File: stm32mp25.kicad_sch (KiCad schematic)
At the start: 0 parts

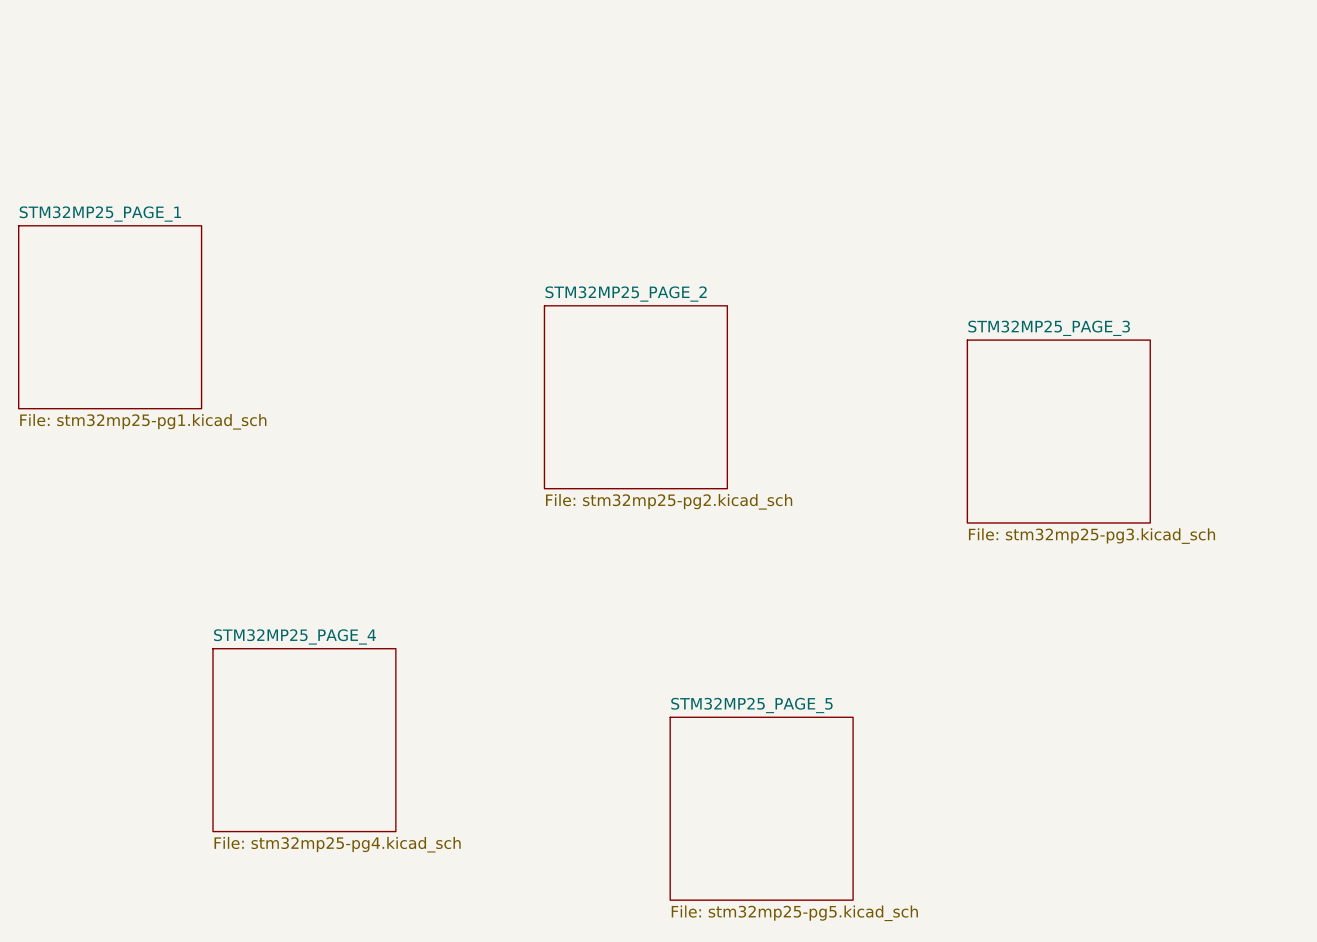
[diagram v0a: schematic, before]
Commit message: connected lpddr4 to mp
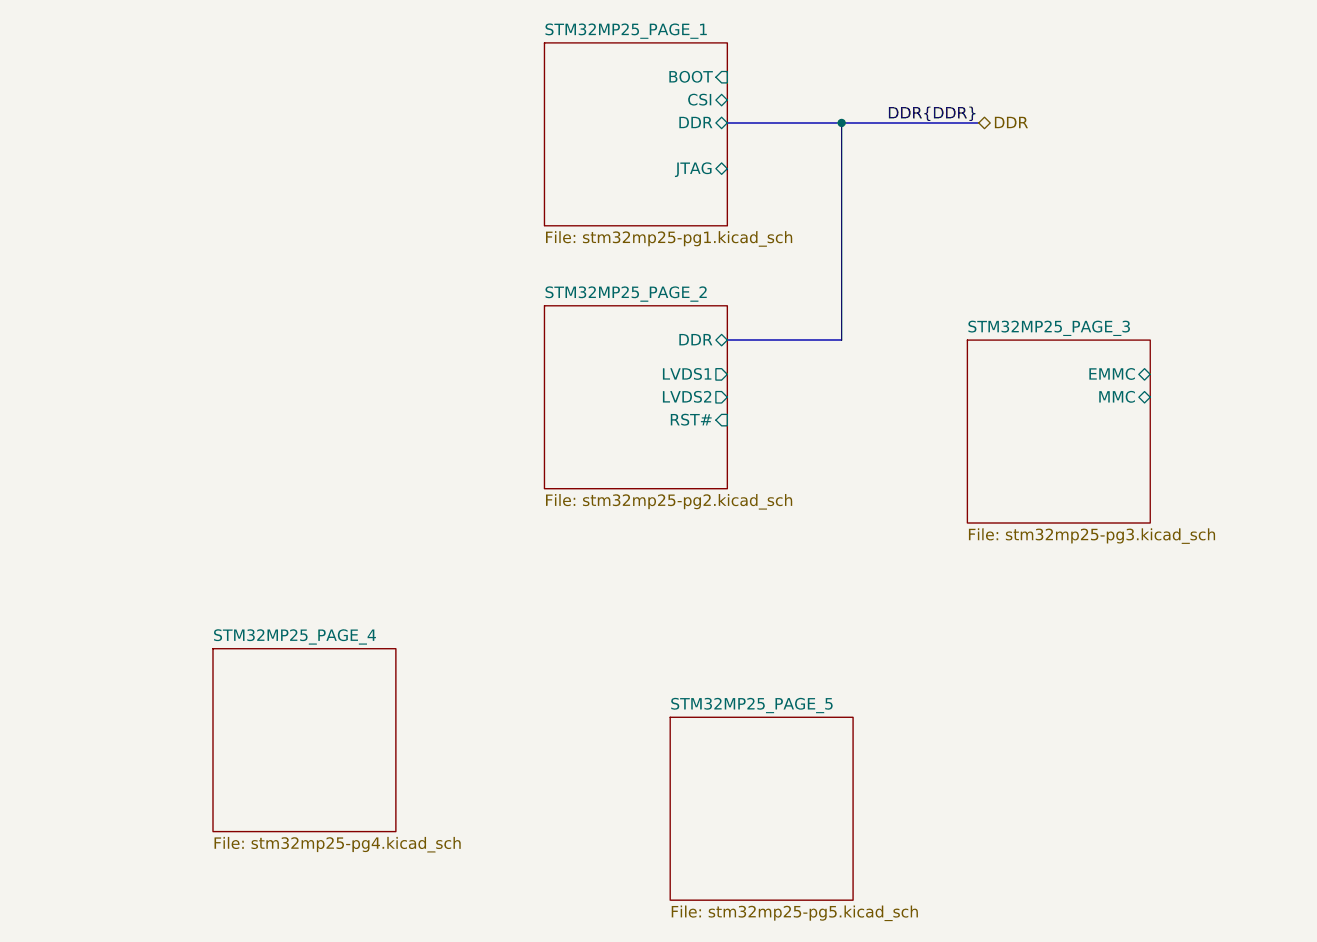
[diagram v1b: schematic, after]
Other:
- sheet STM32MP25_PAGE_1 ports: added BOOT, CSI, DDR, JTAG; removed none
- sheet STM32MP25_PAGE_2 ports: added DDR, LVDS1, LVDS2, RST#; removed none
- sheet STM32MP25_PAGE_3 ports: added EMMC, MMC; removed none
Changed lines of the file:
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@@
 	(generator_version "9.0")
 	(paper "A4")
+	(junction
+		(at 179.07 52.07)
+		(diameter 0)
+		(color 0 0 0 0)
+	)
+	(bus
+		(pts
+			(xy 179.07 52.07) (xy 194.31 52.07)
+		)
+		(stroke
+			(width 0)
+			(type default)
+		)
+	)
+	(bus
+		(pts
+			(xy 179.07 76.2) (xy 179.07 52.07)
+		)
+		(stroke
+			(width 0)
+			(type default)
+		)
+	)
+	(bus
+		(pts
+			(xy 179.07 52.07) (xy 166.37 52.07)
+		)
+		(stroke
+			(width 0)
+			(type default)
+		)
+	)
+	(bus
+		(pts
+			(xy 166.37 76.2) (xy 179.07 76.2)
+		)
+		(stroke
+			(width 0)
+			(type default)
+		)
+	)
+	(label "DDR{DDR}"
+		(at 184.15 52.07 0)
+		(effects
+			(font
+				(size 1.27 1.27)
+			)
+			(justify left bottom)
+		)
+	)
+	(hierarchical_label "DDR"
+		(shape bidirectional)
+		(at 194.31 52.07 0)
+		(effects
+			(font
+				(size 1.27 1.27)
+			)
+			(justify left)
+		)
+	)
 	(sheet
 		(at 146.05 72.39)
@@
 				)
 				(justify left top)
+			)
+		)
+		(pin "DDR" bidirectional
+			(at 166.37 76.2 0)
+			(effects
+				(font
+					(size 1.27 1.27)
+				)
+				(justify right)
+			)
+		)
+		(pin "LVDS1" output
+			(at 166.37 80.01 0)
+			(effects
+				(font
+					(size 1.27 1.27)
+				)
+				(justify right)
+			)
+		)
+		(pin "LVDS2" output
+			(at 166.37 82.55 0)
+			(effects
+				(font
+					(size 1.27 1.27)
+				)
+				(justify right)
+			)
+		)
+		(pin "RST#" input
+			(at 166.37 85.09 0)
+			(effects
+				(font
+					(size 1.27 1.27)
+				)
+				(justify right)
 			)
 		)
@@
 	)
 	(sheet
-		(at 87.63 63.5)
+		(at 146.05 43.18)
 		(size 20.32 20.32)
 		(exclude_from_sim no)
@@
 		)
 		(property "Sheetname" "STM32MP25_PAGE_1"
-			(at 87.63 62.7884 0)
+			(at 146.05 42.4684 0)
 			(effects
 				(font
@@
 		)
 		(property "Sheetfile" "stm32mp25-pg1.kicad_sch"
-			(at 87.63 84.4046 0)
-			(effects
-				(font
-					(size 1.27 1.27)
-				)
-				(justify left top)
+			(at 146.05 64.0846 0)
+			(effects
+				(font
+					(size 1.27 1.27)
+				)
+				(justify left top)
+			)
+		)
+		(pin "BOOT" input
+			(at 166.37 46.99 0)
+			(effects
+				(font
+					(size 1.27 1.27)
+				)
+				(justify right)
+			)
+		)
+		(pin "CSI" bidirectional
+			(at 166.37 49.53 0)
+			(effects
+				(font
+					(size 1.27 1.27)
+				)
+				(justify right)
+			)
+		)
+		(pin "DDR" bidirectional
+			(at 166.37 52.07 0)
+			(effects
+				(font
+					(size 1.27 1.27)
+				)
+				(justify right)
+			)
+		)
+		(pin "JTAG" bidirectional
+			(at 166.37 57.15 0)
+			(effects
+				(font
+					(size 1.27 1.27)
+				)
+				(justify right)
 			)
 		)
@@
 			)
 		)
+		(pin "EMMC" bidirectional
+			(at 213.36 80.01 0)
+			(effects
+				(font
+					(size 1.27 1.27)
+				)
+				(justify right)
+			)
+		)
+		(pin "MMC" bidirectional
+			(at 213.36 82.55 0)
+			(effects
+				(font
+					(size 1.27 1.27)
+				)
+				(justify right)
+			)
+		)
